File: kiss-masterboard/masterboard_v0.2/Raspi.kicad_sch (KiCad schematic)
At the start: 3 parts, among them P2 CONN_02X20

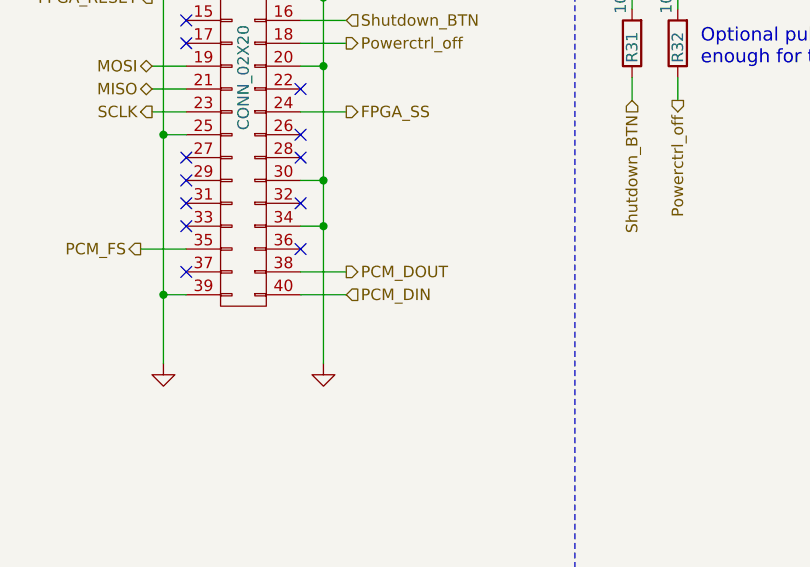
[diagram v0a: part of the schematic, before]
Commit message: Adjust to new batterypack,
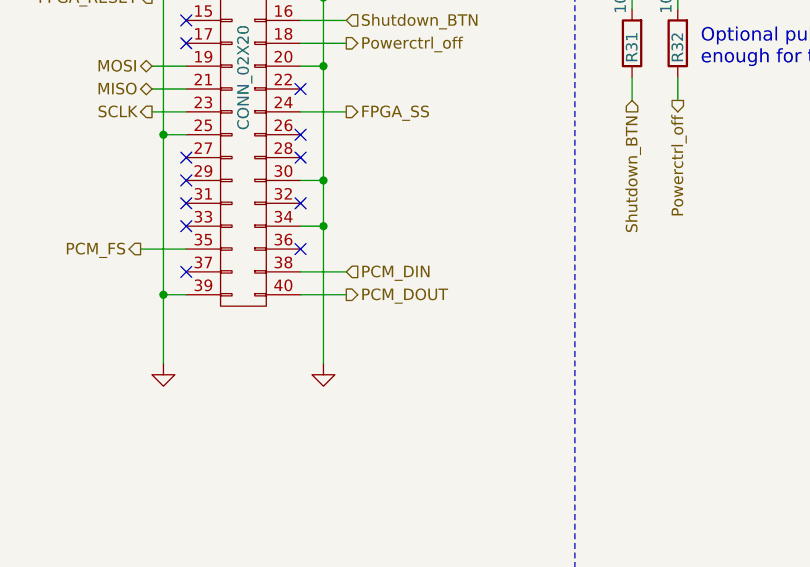
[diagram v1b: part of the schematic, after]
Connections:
- net PCM_DIN: now also P2.38 (P38); no longer P2.40 (P40)
- net PCM_DOUT: now also P2.40 (P40); no longer P2.38 (P38)
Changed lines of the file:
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@@
 	(hierarchical_label "PCM_DOUT"
 		(shape output)
-		(at 60.96 73.66 0)
+		(at 60.96 76.2 0)
 		(effects
 			(font
@@
 	(hierarchical_label "PCM_DIN"
 		(shape input)
-		(at 60.96 76.2 0)
+		(at 60.96 73.66 0)
 		(effects
 			(font

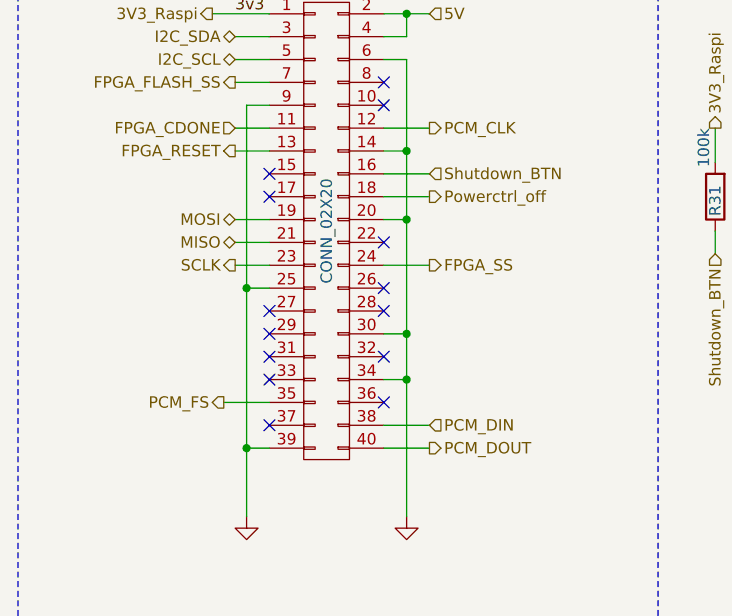
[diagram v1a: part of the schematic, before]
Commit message: Add extension header
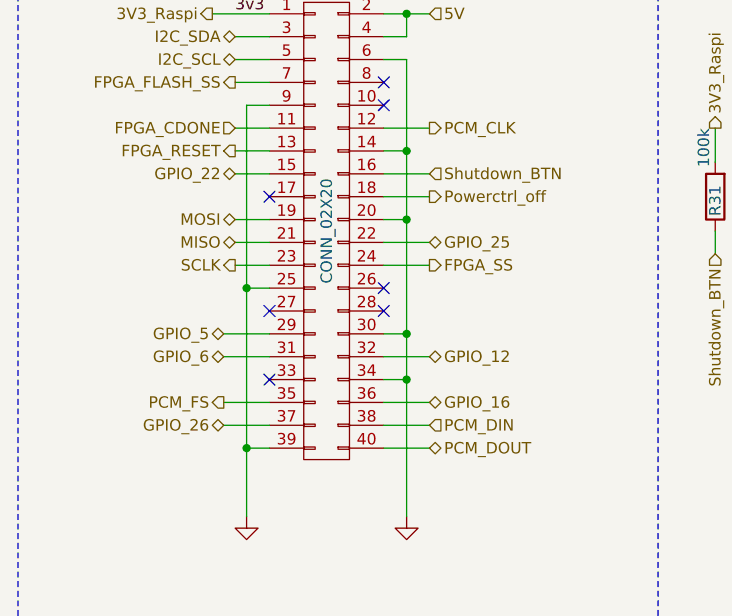
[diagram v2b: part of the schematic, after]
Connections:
- net GPIO_22: now reaches P2.15 (P15)
- net GPIO_25: now reaches P2.22 (P22)
- net GPIO_5: now reaches P2.29 (P29)
- net GPIO_6: now reaches P2.31 (P31)
- net GPIO_12: now reaches P2.32 (P32)
- net GPIO_16: now reaches P2.36 (P36)
- net GPIO_26: now reaches P2.37 (P37)
- no-connect marks 14 -> 7
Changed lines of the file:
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@@
-	)
-	(no_connect
-		(at 43.18 63.5)
-	)
-	(no_connect
-		(at 43.18 66.04)
-	)
-	(no_connect
-		(at 55.88 66.04)
 	)
 	(no_connect
@@
 	)
 	(no_connect
-		(at 43.18 45.72)
-	)
-	(no_connect
 		(at 55.88 35.56)
 	)
@@
 	)
 	(no_connect
-		(at 55.88 53.34)
-	)
-	(no_connect
 		(at 55.88 60.96)
 	)
@@
 		(at 43.18 68.58)
 	)
-	(no_connect
-		(at 55.88 71.12)
-	)
-	(no_connect
-		(at 43.18 73.66)
-	)
 	(polyline
 		(pts
@@
 	(wire
 		(pts
+			(xy 55.88 53.34) (xy 60.96 53.34)
+		)
+		(stroke
+			(width 0)
+			(type default)
+		)
+	)
+	(wire
+		(pts
 			(xy 58.42 68.58) (xy 58.42 83.82)
 		)
@@
 	(wire
 		(pts
+			(xy 38.1 66.04) (xy 43.18 66.04)
+		)
+		(stroke
+			(width 0)
+			(type default)
+		)
+	)
+	(wire
+		(pts
 			(xy 43.18 38.1) (xy 40.64 38.1)
 		)
@@
 	(wire
 		(pts
+			(xy 55.88 71.12) (xy 60.96 71.12)
+		)
+		(stroke
+			(width 0)
+			(type default)
+		)
+	)
+	(wire
+		(pts
 			(xy 43.18 76.2) (xy 40.64 76.2)
 		)
@@
 	(wire
 		(pts
+			(xy 38.1 63.5) (xy 43.18 63.5)
+		)
+		(stroke
+			(width 0)
+			(type default)
+		)
+	)
+	(wire
+		(pts
 			(xy 55.88 27.94) (xy 58.42 27.94)
 		)
@@
 	(wire
 		(pts
+			(xy 55.88 66.04) (xy 60.96 66.04)
+		)
+		(stroke
+			(width 0)
+			(type default)
+		)
+	)
+	(wire
+		(pts
 			(xy 39.37 43.18) (xy 43.18 43.18)
 		)
@@
 	(wire
 		(pts
+			(xy 39.37 45.72) (xy 43.18 45.72)
+		)
+		(stroke
+			(width 0)
+			(type default)
+		)
+	)
+	(wire
+		(pts
 			(xy 55.88 33.02) (xy 58.42 33.02)
 		)
@@
 		(pts
 			(xy 43.18 58.42) (xy 40.64 58.42)
+		)
+		(stroke
+			(width 0)
+			(type default)
+		)
+	)
+	(wire
+		(pts
+			(xy 38.1 73.66) (xy 43.18 73.66)
 		)
 		(stroke
@@
 		)
 	)
+	(hierarchical_label "GPIO_12"
+		(shape bidirectional)
+		(at 60.96 66.04 0)
+		(effects
+			(font
+				(size 1.27 1.27)
+			)
+			(justify left)
+		)
+	)
 	(hierarchical_label "3V3_Raspi"
 		(shape output)
@@
 	)
 	(hierarchical_label "PCM_DOUT"
-		(shape output)
+		(shape bidirectional)
 		(at 60.96 76.2 0)
 		(effects
@@
 			)
 			(justify left)
+		)
+	)
+	(hierarchical_label "GPIO_5"
+		(shape bidirectional)
+		(at 38.1 63.5 180)
+		(effects
+			(font
+				(size 1.27 1.27)
+			)
+			(justify right)
 		)
 	)
@@
 		)
 	)
+	(hierarchical_label "GPIO_26"
+		(shape bidirectional)
+		(at 38.1 73.66 180)
+		(effects
+			(font
+				(size 1.27 1.27)
+			)
+			(justify right)
+		)
+	)
 	(hierarchical_label "I2C_SDA"
 		(shape bidirectional)
@@
 		)
 	)
+	(hierarchical_label "GPIO_16"
+		(shape bidirectional)
+		(at 60.96 71.12 0)
+		(effects
+			(font
+				(size 1.27 1.27)
+			)
+			(justify left)
+		)
+	)
 	(hierarchical_label "3V3_Raspi"
 		(shape output)
 		(at 97.79 40.64 90)
+		(effects
+			(font
+				(size 1.27 1.27)
+			)
+			(justify left)
+		)
+	)
+	(hierarchical_label "GPIO_25"
+		(shape bidirectional)
+		(at 60.96 53.34 0)
 		(effects
 			(font
@@
 		)
 	)
+	(hierarchical_label "GPIO_6"
+		(shape bidirectional)
+		(at 38.1 66.04 180)
+		(effects
+			(font
+				(size 1.27 1.27)
+			)
+			(justify right)
+		)
+	)
 	(hierarchical_label "FPGA_SS"
 		(shape output)
@@
 		(effects
 			(font
+				(size 1.27 1.27)
+			)
+			(justify right)
+		)
+	)
+	(hierarchical_label "GPIO_22"
+		(shape bidirectional)
+		(at 39.37 45.72 180)
+		(effects
+			(font

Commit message: add cnumbers initial order v04a
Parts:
- P2: JLCNR (none) -> C22436166
- R31, R32: JLCNR (none) -> C25803
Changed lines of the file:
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@@
+			)
+		)
+		(property "JLCNR" "C25803"
+			(at 92.71 48.26 90)
+			(hide yes)
+			(show_name no)
+			(do_not_autoplace no)
+			(effects
+				(font
+					(size 3.9878 3.9878)
+				)
 			)
 		)
@@
 			)
 		)
+		(property "JLCNR" "C25803"
+			(at 97.79 48.26 90)
+			(hide yes)
+			(show_name no)
+			(do_not_autoplace no)
+			(effects
+				(font
+					(size 3.9878 3.9878)
+				)
+			)
+		)
 		(pin "1"
 		)
@@
 				)
 			)
+		)
+		(property "JLCNR" "C22436166"
+			(at 49.53 52.07 0)
+			(hide yes)
+			(show_name no)
+			(do_not_autoplace no)
+			(effects
+				(font
+					(size 3.9878 3.9878)
+				)
+			)
